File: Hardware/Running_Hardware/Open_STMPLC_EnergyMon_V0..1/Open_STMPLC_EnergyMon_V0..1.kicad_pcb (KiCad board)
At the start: 2 copper layers, 100 parts, among them J1 Conn_02x08_Odd_Even, J2 Screw_Terminal_01x03, U1 ATM90E36A, U2 ISO7762FDBQ, U5 AMS1117-3.3, Y1 16.384MHz

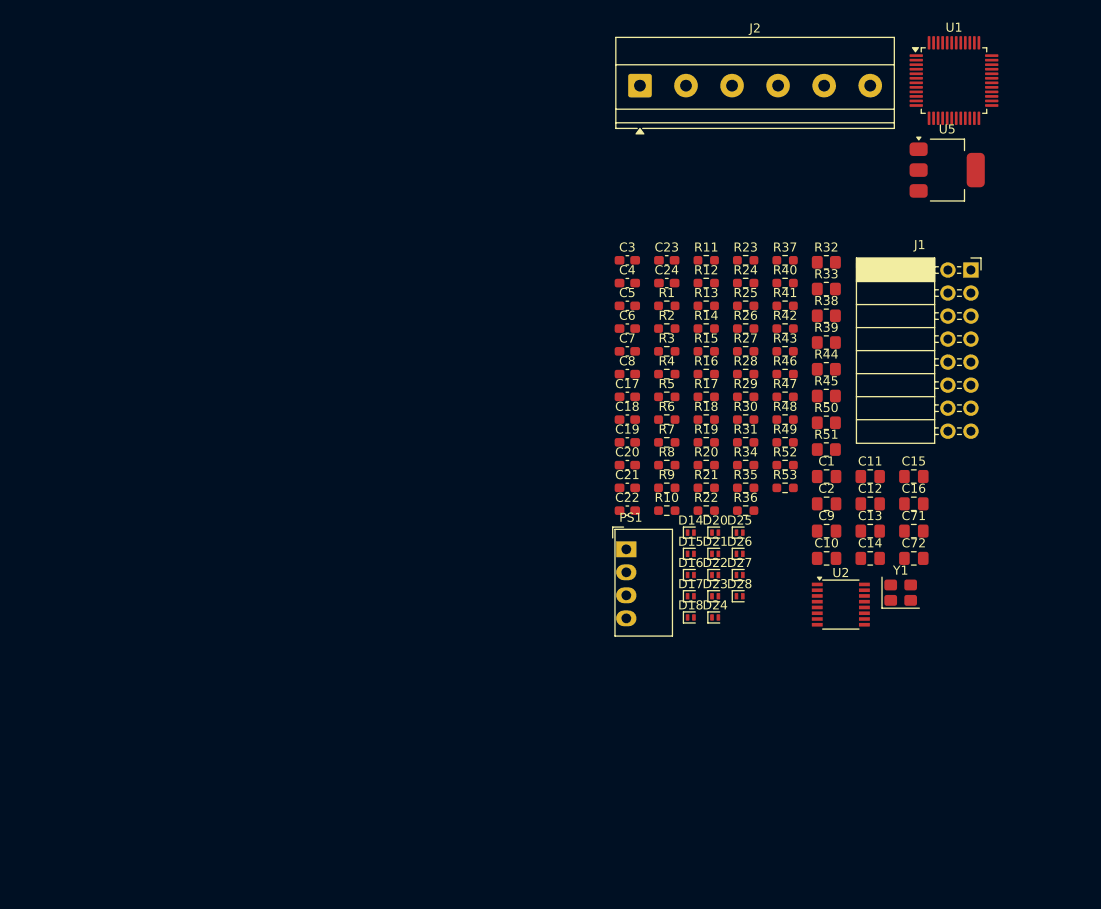
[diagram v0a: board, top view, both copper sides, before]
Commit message: Energy monitoring component grouping
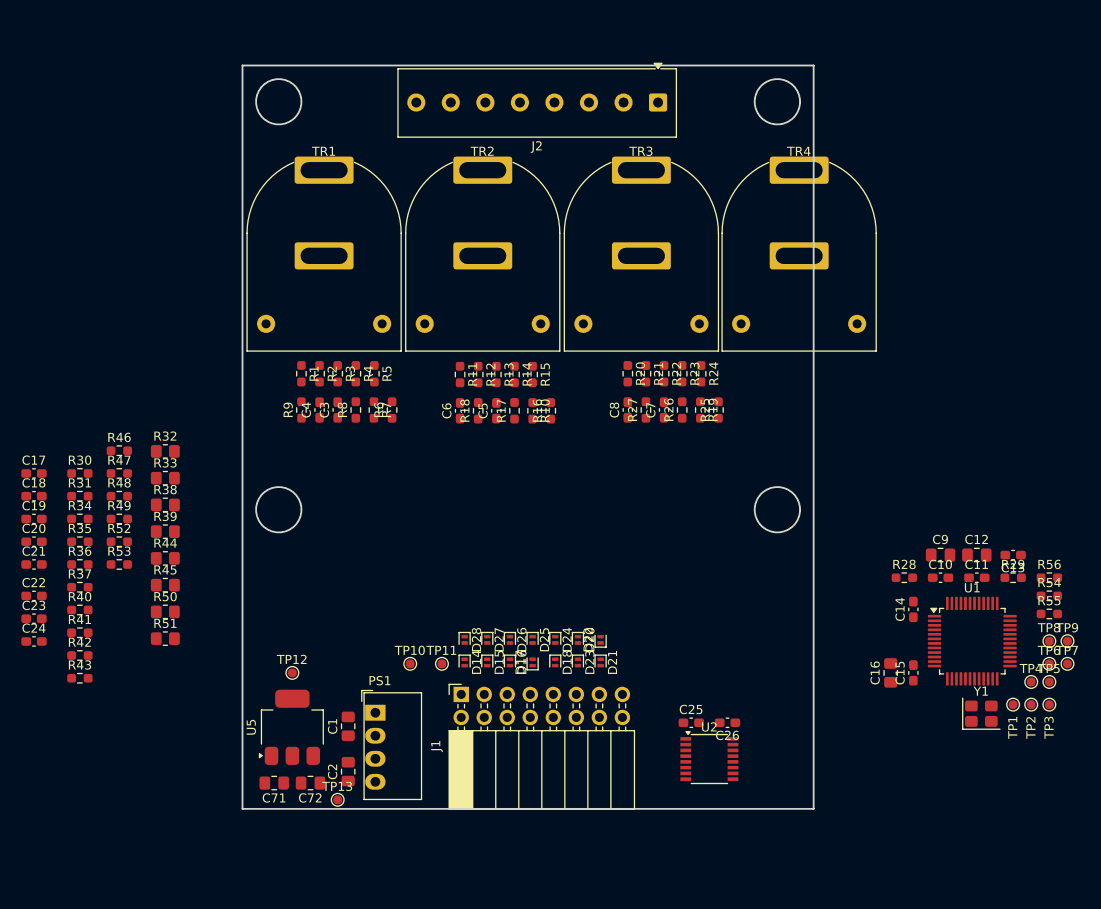
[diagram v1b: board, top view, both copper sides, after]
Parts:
- added C25: 100nF, Capacitor_SMD:C_0603_1608Metric_Pad1.08x0.95mm_HandSolder, F.Cu at (139.5, 130.5)
- added C26: 100nF, Capacitor_SMD:C_0603_1608Metric_Pad1.08x0.95mm_HandSolder, F.Cu at (143.5, 130.5)
- added R54: 10K, Resistor_SMD:R_0603_1608Metric_Pad0.98x0.95mm_HandSolder, F.Cu at (179.0, 116.5)
- added R55: 10K, Resistor_SMD:R_0603_1608Metric_Pad0.98x0.95mm_HandSolder, F.Cu at (179.0, 118.5)
- added R56: 10K, Resistor_SMD:R_0603_1608Metric_Pad0.98x0.95mm_HandSolder, F.Cu at (179.0, 114.5)
- added TP1: TestPoint, TestPoint:TestPoint_Pad_D1.0mm, F.Cu at (175.0, 128.5)
- added TP10: TestPoint, TestPoint:TestPoint_Pad_D1.0mm, F.Cu at (108.5, 124.0)
- added TP11: TestPoint, TestPoint:TestPoint_Pad_D1.0mm, F.Cu at (112.0, 124.0)
- added TP12: TestPoint, TestPoint:TestPoint_Pad_D1.0mm, F.Cu at (95.5, 125.0)
- added TP13: TestPoint, TestPoint:TestPoint_Pad_D1.0mm, F.Cu at (100.5, 139.0)
- added TP2: TestPoint, TestPoint:TestPoint_Pad_D1.0mm, F.Cu at (177.0, 128.5)
- added TP3: TestPoint, TestPoint:TestPoint_Pad_D1.0mm, F.Cu at (179.0, 128.5)
- added TP4: TestPoint, TestPoint:TestPoint_Pad_D1.0mm, F.Cu at (177.0, 126.0)
- added TP5: TestPoint, TestPoint:TestPoint_Pad_D1.0mm, F.Cu at (179.0, 126.0)
- added TP6: TestPoint, TestPoint:TestPoint_Pad_D1.0mm, F.Cu at (179.0, 124.0)
- added TP7: TestPoint, TestPoint:TestPoint_Pad_D1.0mm, F.Cu at (181.0, 124.0)
- added TP8: TestPoint, TestPoint:TestPoint_Pad_D1.0mm, F.Cu at (179.0, 121.5)
- added TP9: TestPoint, TestPoint:TestPoint_Pad_D1.0mm, F.Cu at (181.0, 121.5)
- added TR1: ZHTM104B, Footprints:ZHTM104B, F.Cu at (99.0, 86.5)
- added TR2: ZHTM104B, Footprints:ZHTM104B, F.Cu at (116.5, 86.5)
- added TR3: ZHTM104B, Footprints:ZHTM104B, F.Cu at (134.0, 86.5)
- added TR4: ZHTM104B, Footprints:ZHTM104B, F.Cu at (151.4, 86.5)
- C10, C11, C13, C14, C15: footprint Capacitor_SMD:C_0805_2012Metric_Pad1.18x1.45mm_HandSolder -> Capacitor_SMD:C_0603_1608Metric_Pad1.08x0.95mm_HandSolder
- J2: value Screw_Terminal_01x03 -> Screw_Terminal_01x08; footprint TerminalBlock_Phoenix:TerminalBlock_Phoenix_MKDS-1,5-6-5.08_1x06_P5.08mm_Horizontal -> TerminalBlock_Phoenix:TerminalBlock_Phoenix_MKDS-1-8-3.81_1x08_P3.81mm_Horizontal
- moved U5 94.8 mm to (95.5, 131.0), turned to 90 degrees
- moved R37 85.7 mm to (72.1, 115.5)
- moved R40 85.7 mm to (72.1, 118.1)
- moved R41 85.7 mm to (72.1, 120.6)
- moved R42 85.7 mm to (72.1, 123.1)
- moved R43 85.7 mm to (72.1, 125.6)
- moved C23 80.2 mm to (67.0, 119.0)
- moved C24 80.2 mm to (67.0, 121.5)
- moved R32 75.8 mm to (81.5, 100.6)
- moved R33 75.8 mm to (81.5, 103.5)
- moved R38 75.8 mm to (81.5, 106.5)
- moved R39 75.8 mm to (81.5, 109.4)
- moved R44 75.8 mm to (81.5, 112.4)
- moved R45 75.8 mm to (81.5, 115.3)
- moved R50 75.8 mm to (81.5, 118.3)
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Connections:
- net Net-(J2-Pin_4) renamed /W_IN
- J2 pad 1: unconnected-(J2-Pin_1-Pad1) -> /N_OUT
- J2 pad 2: unconnected-(J2-Pin_2-Pad2) -> /N_IN
- J2 pad 3: unconnected-(J2-Pin_3-Pad3) -> /W_OUT
- J2 pad 5: Net-(J2-Pin_5) -> /V_OUT
- J2 pad 6: Net-(J2-Pin_6) -> /V_IN
- R1 pad 1: Net-(J2-Pin_6) -> /U_IN
- R11 pad 1: Net-(J2-Pin_5) -> /V_IN
- R42 pad 1: unconnected-(R42-Pad1) -> Net-(R42-Pad1)
- R46 pad 1: unconnected-(R46-Pad1) -> Net-(R46-Pad1)
- U2 pad 1: unconnected-(U2-Vcc1-Pad1) -> +3V3
- U2 pad 10: unconnected-(U2-INF-Pad10) -> /IRQ0
- U2 pad 11: unconnected-(U2-INE-Pad11) -> /SDO
- U2 pad 12: unconnected-(U2-OUTD-Pad12) -> /SCLK
- U2 pad 13: unconnected-(U2-OUTC-Pad13) -> /SDI
- U2 pad 14: unconnected-(U2-OUTB-Pad14) -> /EM_CS
- U2 pad 15: unconnected-(U2-OUTA-Pad15) -> /EM_RST
- U2 pad 16: unconnected-(U2-Vcc2-Pad16) -> +3.3VA
- U2 pad 2: unconnected-(U2-INA-Pad2) -> /EX_GPIO1
- U2 pad 3: unconnected-(U2-INB-Pad3) -> /EX_GPIO2
- U2 pad 4: unconnected-(U2-INC-Pad4) -> /EX_SPI_MOSI
- U2 pad 5: unconnected-(U2-IND-Pad5) -> /EX_SPI_CLK
- U2 pad 6: unconnected-(U2-OUTE-Pad6) -> /EX_SPI_MISO
- U2 pad 7: unconnected-(U2-OUTF-Pad7) -> /EX_GPIO3
- U2 pad 8: unconnected-(U2-GND1-Pad8) -> GND
- U2 pad 9: unconnected-(U2-GND2-Pad9) -> GNDA
- Y1 pad 2: Net-(U1-OSCO) -> GNDA
- Y1 pad 3: (no net) -> Net-(U1-OSCO)
- Y1 pad 4: (no net) -> GNDA
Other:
- board outline added: 63 x 82 mm

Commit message: Energy monitoring layout
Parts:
- added H1: MountingHole, MountingHole:MountingHole_3.2mm_M3, F.Cu at (94.0, 64.0)
- added H2: MountingHole, MountingHole:MountingHole_3.2mm_M3, F.Cu at (156.0, 64.0)
- added H3: MountingHole, MountingHole:MountingHole_3.2mm_M3, F.Cu at (94.0, 136.0)
- added H4: MountingHole, MountingHole:MountingHole_3.2mm_M3, F.Cu at (156.0, 136.0)
- J1: footprint Connector_PinSocket_2.54mm:PinSocket_2x08_P2.54mm_Horizontal -> Connector_PinHeader_2.54mm:PinHeader_2x08_P2.54mm_Horizontal
- moved C18 86.0 mm to (153.0, 108.0)
- moved R31 85.0 mm to (157.0, 103.0), turned to 180 degrees
- moved C17 82.2 mm to (149.0, 108.0), turned to 180 degrees
- moved R35 81.1 mm to (153.0, 106.0)
- moved R34 77.0 mm to (149.0, 106.0), turned to 180 degrees
- moved R30 72.9 mm to (145.0, 103.0)
- moved R33 71.5 mm to (153.0, 103.0), turned to 180 degrees
- moved R40 69.6 mm to (140.0, 103.0), turned to 180 degrees
- moved C20 69.0 mm to (136.0, 108.0)
- moved R32 67.6 mm to (149.0, 103.0), turned to 180 degrees
- moved R41 65.6 mm to (136.0, 106.0)
- moved C19 65.0 mm to (132.0, 108.0), turned to 180 degrees
- moved R37 60.7 mm to (132.0, 106.0), turned to 180 degrees
- moved R36 56.8 mm to (128.0, 103.0)
- moved R39 54.9 mm to (136.0, 103.0), turned to 180 degrees
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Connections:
- C26 pad 2: GND -> GNDA
- J2 pad 1: /N_OUT -> /U_IN
- J2 pad 2: /N_IN -> /U_OUT
- J2 pad 3: /W_OUT -> /V_IN
- J2 pad 4: /W_IN -> /V_OUT
- J2 pad 5: /V_OUT -> /W_OUT
- J2 pad 6: /V_IN -> /W_IN
- J2 pad 7: /U_OUT -> /N_OUT
- J2 pad 8: /U_IN -> /N_IN
- U2 pad 10: /IRQ0 -> /SDO
- U2 pad 11: /SDO -> /SCLK
- U2 pad 12: /SCLK -> /SDI
- U2 pad 13: /SDI -> /IRQ0
- U2 pad 2: /EX_GPIO1 -> /EX_GPIO3
- U2 pad 4: /EX_SPI_MOSI -> /EX_GPIO1
- U2 pad 5: /EX_SPI_CLK -> /EX_SPI_MOSI
- U2 pad 6: /EX_SPI_MISO -> /EX_SPI_CLK
- U2 pad 7: /EX_GPIO3 -> /EX_SPI_MISO
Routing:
- net +3.3VA: track 0.00 -> 156.1 mm, vias 0 -> 2
- net GNDA: track 0.00 -> 127.5 mm, vias 0 -> 39
- net /VCN: track 0.00 -> 87.5 mm, vias 0 -> 2
- net /VCP: track 0.00 -> 87.3 mm, vias 0 -> 2
- net /VBN: track 0.00 -> 64.1 mm, vias 0 -> 2
- net /VBP: track 0.00 -> 59.6 mm
- net /INP: track 0.00 -> 57.6 mm, vias 0 -> 2
- net +5V: track 0.00 -> 57.1 mm
- net /INN: track 0.00 -> 55.8 mm, vias 0 -> 2
- net /VAP: track 0.00 -> 46.9 mm
- net /VAN: track 0.00 -> 46.5 mm
- net /ICP: track 0.00 -> 39.2 mm, vias 0 -> 2
- net /ICN: track 0.00 -> 37.2 mm, vias 0 -> 2
- net +3V3: track 0.00 -> 33.7 mm, vias 0 -> 1
- net /U_OUT: track 0.00 -> 32.8 mm
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- added copper zone on B.Cu, net GND
- added copper zone on F.Cu, net GND
- added copper zone on B.Cu, net GNDA
- added copper zone on F.Cu, net GNDA
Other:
- board size 63 x 82 mm -> 70 x 80 mm

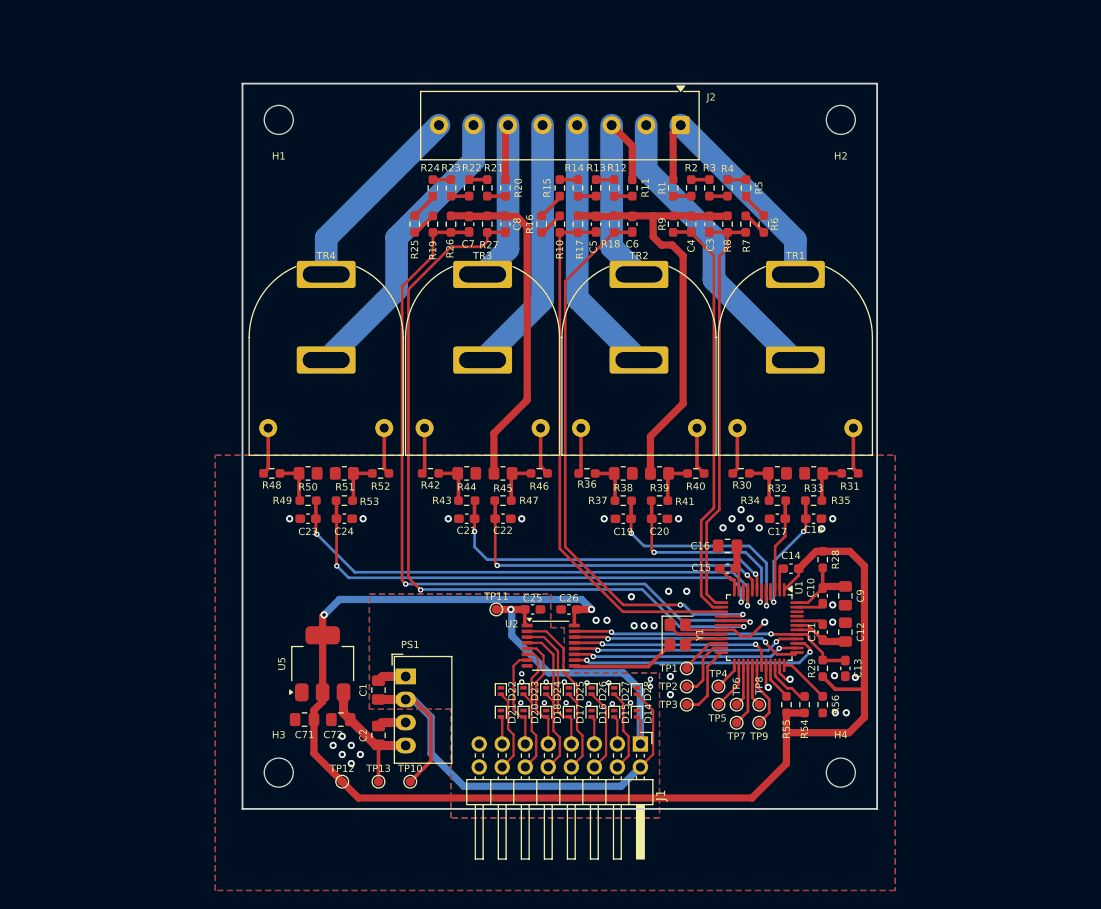
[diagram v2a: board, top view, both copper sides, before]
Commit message: Energy monitoring gerber generated
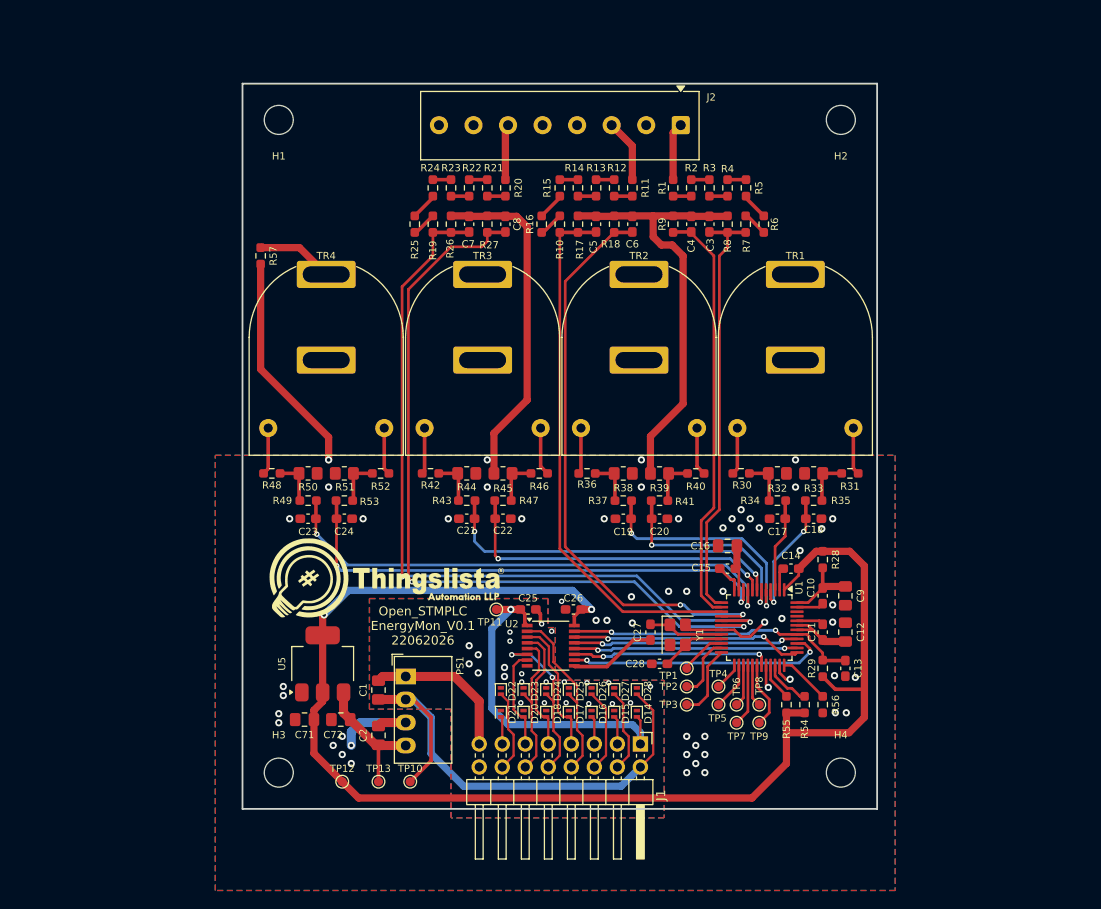
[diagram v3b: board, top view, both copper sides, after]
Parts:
- added C27: 10pF, Capacitor_SMD:C_0603_1608Metric_Pad1.08x0.95mm_HandSolder, F.Cu at (135.0, 120.5)
- added C28: 10pF, Capacitor_SMD:C_0603_1608Metric_Pad1.08x0.95mm_HandSolder, F.Cu at (136.0, 124.0)
- added G***: LOGO, Footprints:Thingslista, F.Cu at (105.9, 114.5)
- added R57: 0R, Resistor_SMD:R_0603_1608Metric_Pad0.98x0.95mm_HandSolder, F.Cu at (92.0, 79.0)
- moved C25 0.50 mm to (121.5, 118.0)
- moved C26 0.50 mm to (126.5, 118.0)
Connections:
- U2 pad 11: /SCLK -> /IRQ0
- U2 pad 12: /SDI -> /SCLK
- U2 pad 13: /IRQ0 -> /SDI
- U2 pad 4: /EX_GPIO1 -> /EX_SPI_MOSI
- U2 pad 5: /EX_SPI_MOSI -> /EX_SPI_CLK
- U2 pad 6: /EX_SPI_CLK -> /EX_GPIO1
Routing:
- net GNDA: track 127.5 -> 158.2 mm, vias 39 -> 58
- net GND: track 3.19 -> 19.0 mm, vias 14 -> 23
- net /N_IN: track 21.6 -> 30.1 mm
- net +3V3: track 33.7 -> 38.4 mm
- net Net-(U1-OSCO): track 4.26 -> 7.18 mm
- net Net-(U1-OSCI): track 6.21 -> 8.39 mm
- net /EX_GPIO1: track 17.8 -> 19.2 mm, vias 0 -> 2
- net /EX_SPI_CLK: track 15.6 -> 16.5 mm
- net /EX_SPI_MOSI: track 13.0 -> 13.8 mm
- net /IRQ0: track 22.7 -> 22.0 mm
- net +3.3VA: track 156.1 -> 156.7 mm
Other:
- board text added: "N_IN"
- board text added: "N_OUT"
- board text added: "Open_STMPLC EnergyMon_V0.1 22062026"
- board text added: "U_IN"
- board text added: "U_OUT"
- board text added: "V_IN"
- board text added: "V_OUT"
- board text added: "W_IN"
- board text added: "W_OUT"
